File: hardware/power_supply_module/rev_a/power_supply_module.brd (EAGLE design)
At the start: 68.1 x 66 mm, 95 parts, among them J1 MODULE_POWER, U1 TLV62130, U10 LTC2941, U11 LTC2941, U12 LTC2941, U13 LTC2941, U14 LTC2941, U15 LTC2941, U2 TLV62130, U3 TLV62130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

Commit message: switch to recommended 5v resistor divider
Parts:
- R14, R15, R16, R17: value 143k -> 130k
- R20, R21, R22, R23: value 750k -> 680k
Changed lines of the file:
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@@
 <attribute name="NAME" x="39.37" y="4.826" size="1.016" layer="25" font="vector" ratio="12" rot="R270" align="bottom-center"/>
 </element>
-<element name="R21" library="passives" package="0402_RES" value="750k" x="38.735" y="6.35" smashed="yes" rot="R270">
+<element name="R21" library="passives" package="0402_RES" value="680k" x="38.735" y="6.35" smashed="yes" rot="R270">
 <attribute name="NAME" x="39.37" y="7.747" size="1.016" layer="25" font="vector" ratio="12" rot="R270" align="bottom-center"/>
 <attribute name="VALUE" x="37.338" y="6.35" size="1.016" layer="27" font="vector" ratio="12" rot="R270" align="bottom-center"/>
 </element>
-<element name="R15" library="passives" package="0402_RES" value="143k" x="37.465" y="8.89" smashed="yes">
+<element name="R15" library="passives" package="0402_RES" value="130k" x="37.465" y="8.89" smashed="yes">
 <attribute name="NAME" x="37.465" y="9.271" size="1.016" layer="25" font="vector" ratio="12" align="bottom-center"/>
 <attribute name="VALUE" x="37.465" y="7.493" size="1.016" layer="27" font="vector" ratio="12" align="bottom-center"/>
@@
 <attribute name="NAME" x="29.718" y="4.699" size="1.016" layer="25" font="vector" ratio="12" rot="R270" align="bottom-center"/>
 </element>
-<element name="R20" library="passives" package="0402_RES" value="750k" x="29.21" y="6.35" smashed="yes" rot="R270">
+<element name="R20" library="passives" package="0402_RES" value="680k" x="29.21" y="6.35" smashed="yes" rot="R270">
 <attribute name="NAME" x="29.591" y="7.62" size="1.016" layer="25" font="vector" ratio="12" rot="R270" align="bottom-center"/>
 <attribute name="VALUE" x="27.813" y="6.35" size="1.016" layer="27" font="vector" ratio="12" rot="R270" align="bottom-center"/>
 </element>
-<element name="R14" library="passives" package="0402_RES" value="143k" x="27.94" y="8.89" smashed="yes">
+<element name="R14" library="passives" package="0402_RES" value="130k" x="27.94" y="8.89" smashed="yes">
 <attribute name="NAME" x="27.94" y="9.271" size="1.016" layer="25" font="vector" ratio="12" align="bottom-center"/>
 <attribute name="VALUE" x="27.94" y="7.493" size="1.016" layer="27" font="vector" ratio="12" align="bottom-center"/>
@@
 <attribute name="NAME" x="49.022" y="2.794" size="1.016" layer="25" font="vector" ratio="12" rot="R180" align="bottom-center"/>
 </element>
-<element name="R22" library="passives" package="0402_RES" value="750k" x="48.895" y="6.35" smashed="yes" rot="R270">
+<element name="R22" library="passives" package="0402_RES" value="680k" x="48.895" y="6.35" smashed="yes" rot="R270">
 <attribute name="NAME" x="49.276" y="6.35" size="1.016" layer="25" font="vector" ratio="12" rot="R270" align="bottom-center"/>
 <attribute name="VALUE" x="47.498" y="6.35" size="1.016" layer="27" font="vector" ratio="12" rot="R270" align="bottom-center"/>
 </element>
-<element name="R16" library="passives" package="0402_RES" value="143k" x="47.625" y="8.89" smashed="yes">
+<element name="R16" library="passives" package="0402_RES" value="130k" x="47.625" y="8.89" smashed="yes">
 <attribute name="NAME" x="47.625" y="9.271" size="1.016" layer="25" font="vector" ratio="12" align="bottom-center"/>
 <attribute name="VALUE" x="47.625" y="7.493" size="1.016" layer="27" font="vector" ratio="12" align="bottom-center"/>
@@
 <attribute name="NAME" x="56.896" y="9.144" size="1.016" layer="25" font="vector" ratio="12" rot="R180" align="bottom-center"/>
 </element>
-<element name="R23" library="passives" package="0402_RES" value="750k" x="57.15" y="12.7" smashed="yes" rot="R270">
+<element name="R23" library="passives" package="0402_RES" value="680k" x="57.15" y="12.7" smashed="yes" rot="R270">
 <attribute name="NAME" x="57.531" y="12.7" size="1.016" layer="25" font="vector" ratio="12" rot="R270" align="bottom-center"/>
 <attribute name="VALUE" x="55.753" y="12.7" size="1.016" layer="27" font="vector" ratio="12" rot="R270" align="bottom-center"/>
 </element>
-<element name="R17" library="passives" package="0402_RES" value="143k" x="55.88" y="15.24" smashed="yes">
+<element name="R17" library="passives" package="0402_RES" value="130k" x="55.88" y="15.24" smashed="yes">
 <attribute name="NAME" x="55.88" y="15.621" size="1.016" layer="25" font="vector" ratio="12" align="bottom-center"/>
 <attribute name="VALUE" x="55.88" y="13.843" size="1.016" layer="27" font="vector" ratio="12" align="bottom-center"/>

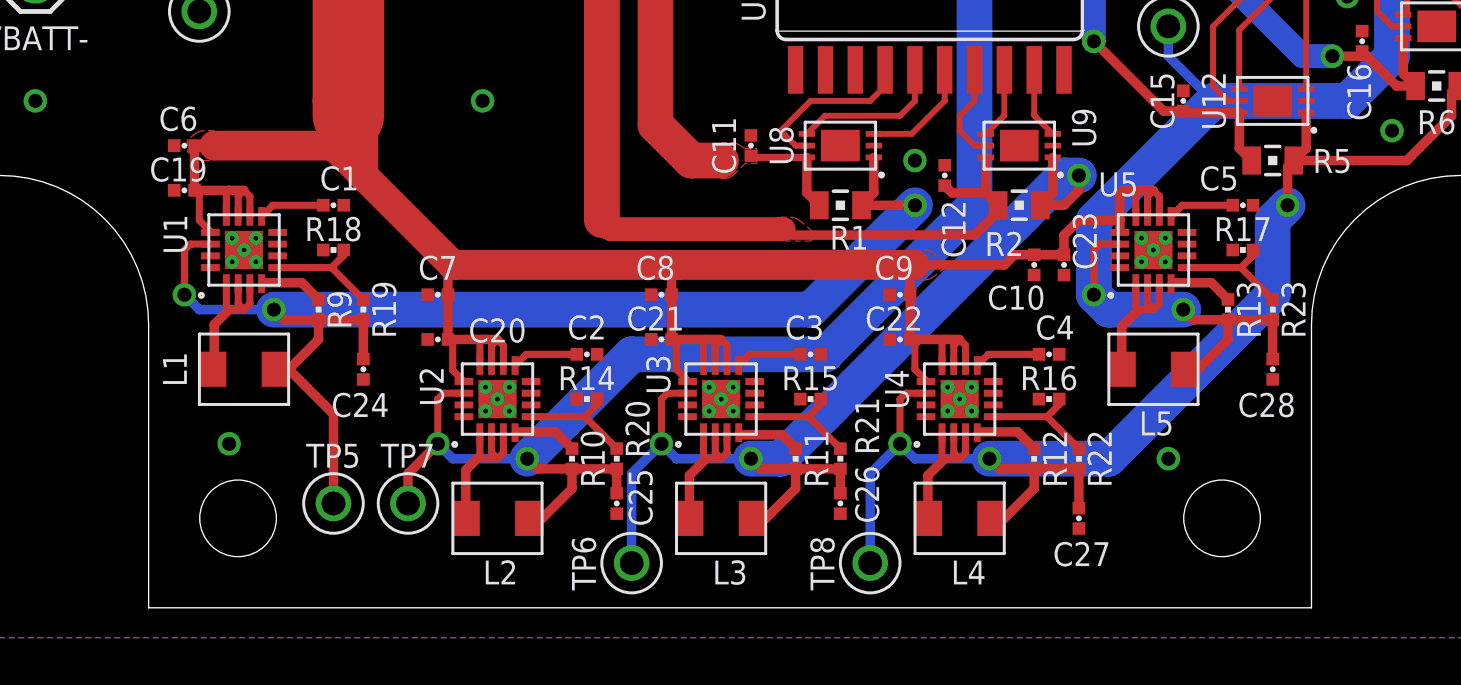
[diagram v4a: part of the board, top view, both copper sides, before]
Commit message: Added bom, resized high voltage, large value caps
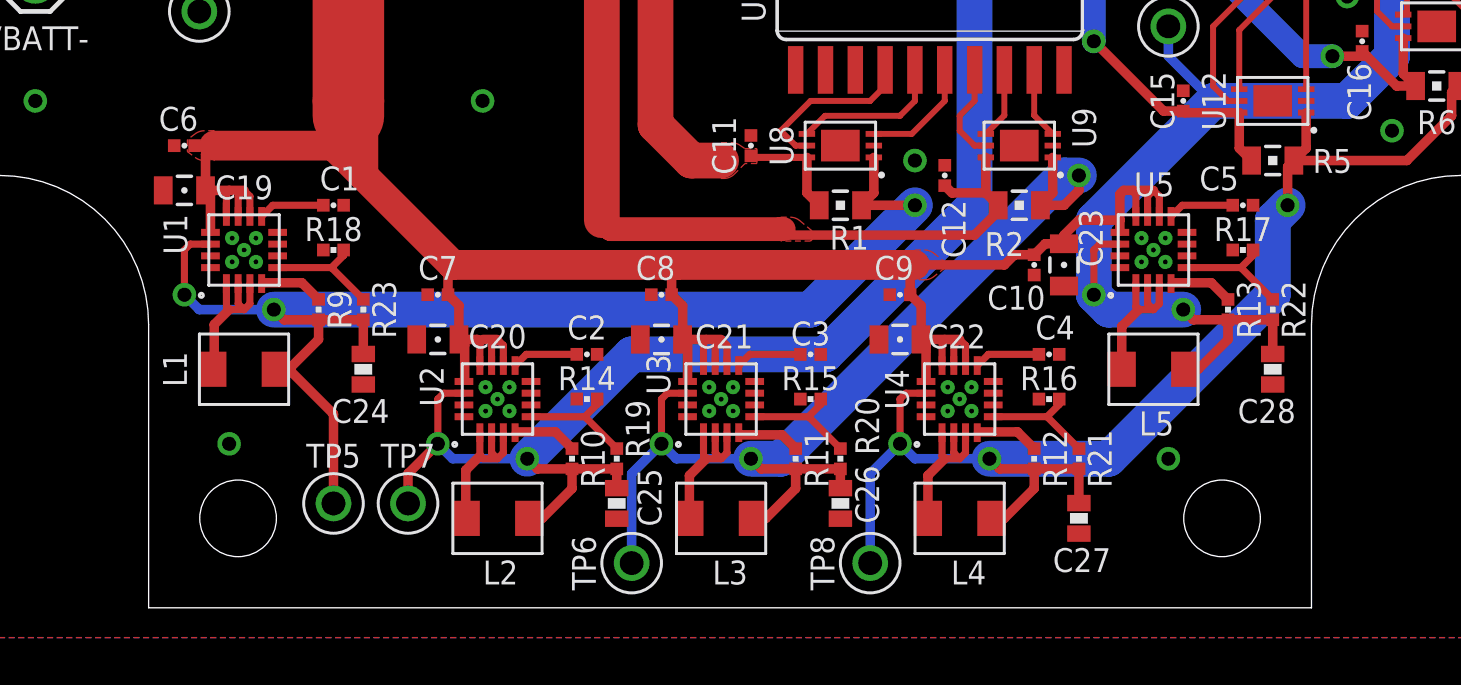
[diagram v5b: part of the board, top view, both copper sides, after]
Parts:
- C1, C2, C3, C4, C5: value 3.3nF -> 3.3n
- C10, C6, C7, C8, C9: value 0.1uF -> 0.1u
- C19, C20, C21, C22, C23: value 10uF -> 10u; device passives:0402_CAP -> passives:0805_CAP
- C24, C25, C26, C27, C28: value 22uF -> 22u; device passives:0402_CAP -> passives:0603_CAP
- L1, L2, L3, L4, L5: value 2.2uH -> 2.2u
- R10, R11, R12, R13, R9: value 100K -> 100k
- R19: value 750k -> 680k
- R23: value 680k -> 750k
- moved R23 38.7 mm to (18.4, 12.7)
- moved R19 12.5 mm to (29.2, 6.35)
- moved R22 10.4 mm to (57.1, 12.7)
- moved R21 10.2 mm to (48.9, 6.35)
- moved R20 9.52 mm to (38.7, 6.35)
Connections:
- net 3V3: now also R23.2; no longer R19.2
- net 5V_1: now also R20.2; no longer R21.2
- net 5V_2: now also R19.2; no longer R20.2
- net 5V_3: now also R21.2; no longer R22.2
- net 5V_4: now also R22.2; no longer R23.2
- net GND: no longer U1.GND, U2.GND, U3.GND, U4.GND, U5.GND
- net N$12: now also R21.1; no longer R22.1
- net N$16: now also R22.1; no longer R23.1
- net N$4: now also R19.1; no longer R20.1
- net N$64: now also R23.1; no longer R19.1
- net N$9: now also R20.1; no longer R21.1
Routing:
- net VBATT: track 164.1 -> 162.4 mm

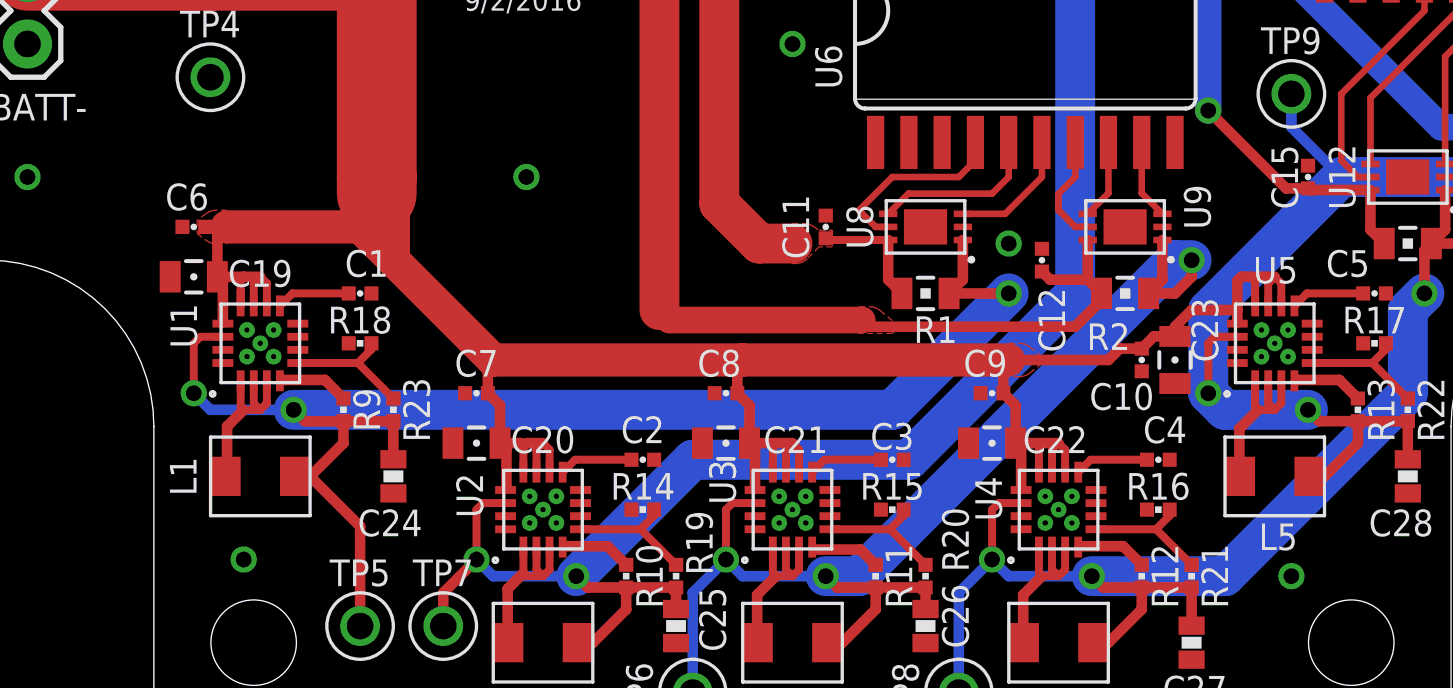
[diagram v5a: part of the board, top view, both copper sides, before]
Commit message: Add files for manufacture. Sent to fab
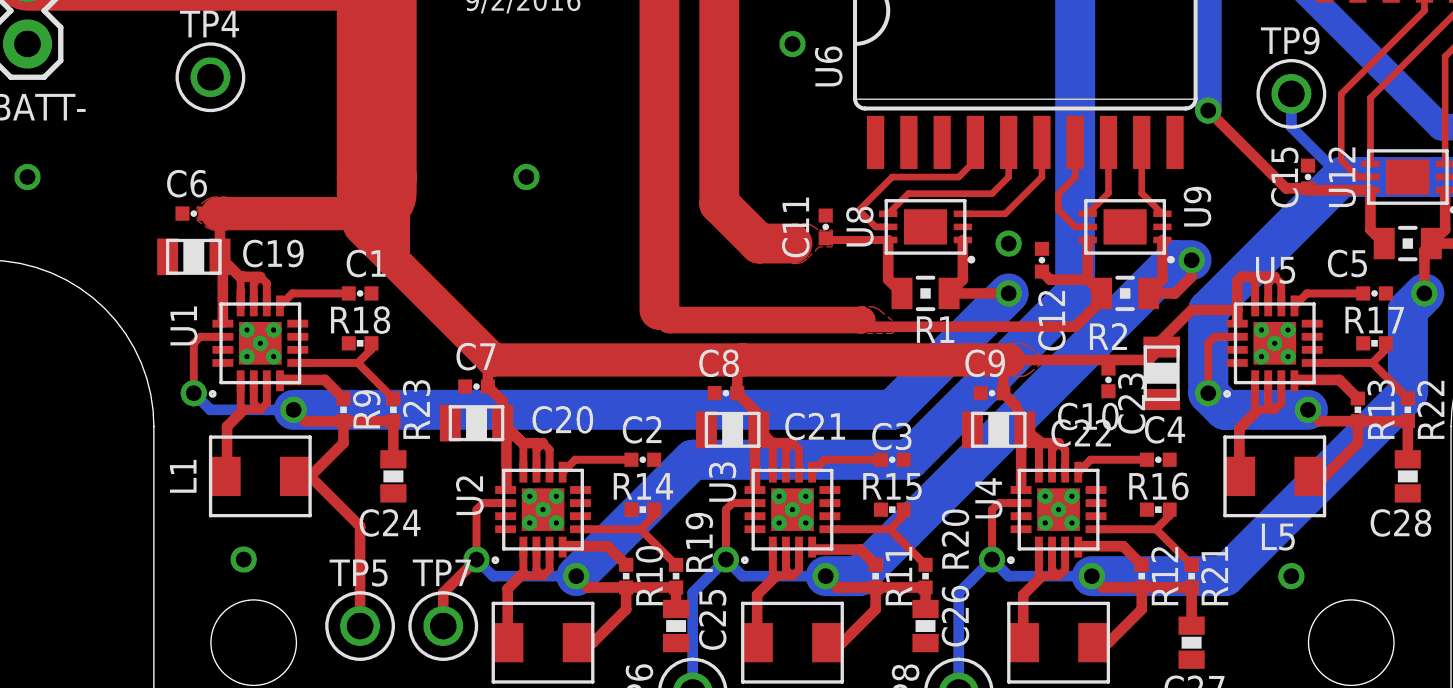
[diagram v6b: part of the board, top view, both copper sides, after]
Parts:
- moved C10 1.48 mm to (45.7, 13.8)
- moved C19 0.76 mm to (10.8, 18.5), turned to 0 degrees
- moved C20 0.76 mm to (21.6, 12.2), turned to 0 degrees
- moved C23 0.72 mm to (47.8, 14.1), turned to 90 degrees
- moved C22 0.57 mm to (41.5, 11.9), turned to 0 degrees
- moved C21 0.57 mm to (31.4, 11.9), turned to 0 degrees
- moved C6 0.51 mm to (10.8, 20.2)
- moved C7 0.25 mm to (21.6, 13.6)
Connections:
- net GND: now also C19.P$2, C20.P$2, C21.P$2, C22.P$2, C23.P$2, U1.GND, U2.GND, U3.GND, U4.GND, U5.GND; no longer C19.2, C20.2, C21.2, C22.2, C23.2
- net VBATT: now also C19.P$1, C20.P$1, C21.P$1, C22.P$1, C23.P$1; no longer C19.1, C20.1, C21.1, C22.1, C23.1
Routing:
- net VBATT: track 162.4 -> 165.1 mm
